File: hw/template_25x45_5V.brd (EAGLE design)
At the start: 25 x 45 mm, 25 parts, among them J1 GROVE-4P-2.0-3470130P1, J2 GROVE-4P-2.0-3470130P1, U5 LD3985XX

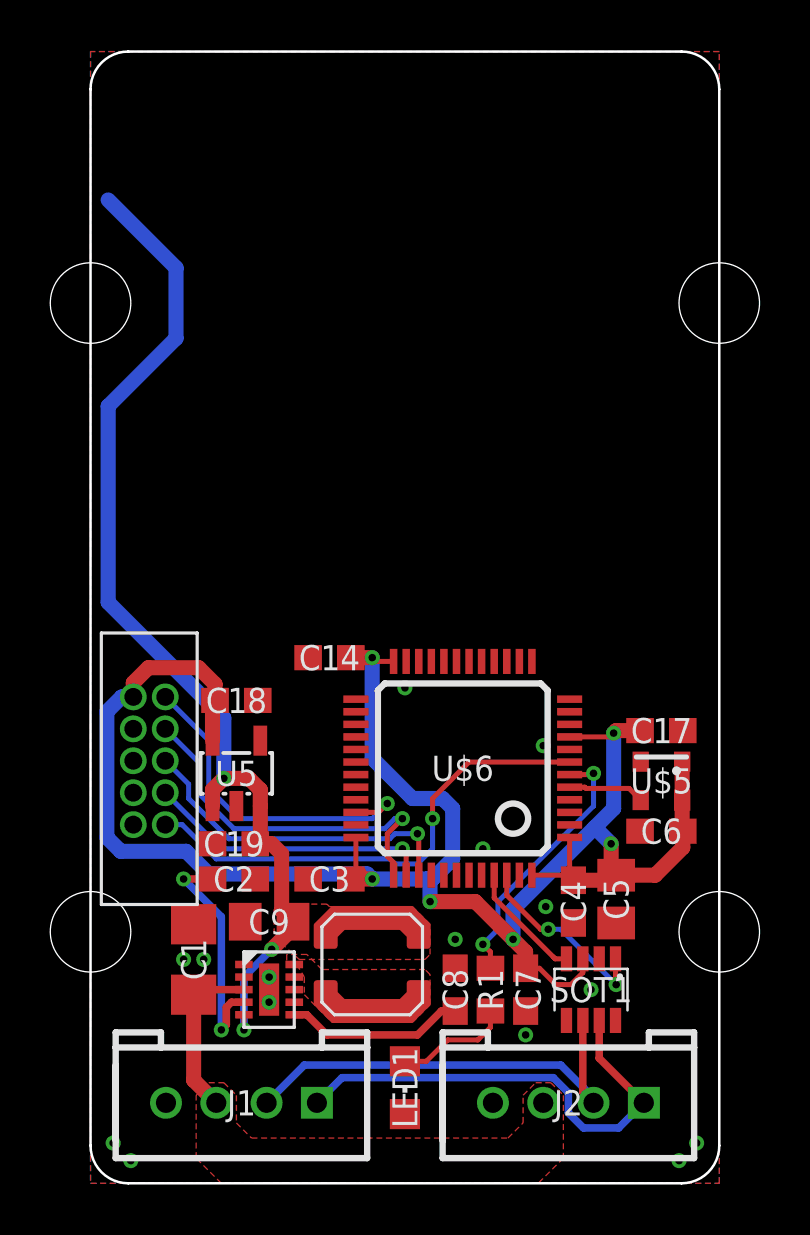
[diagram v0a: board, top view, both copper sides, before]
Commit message: Updated to R2P Eagle libraries
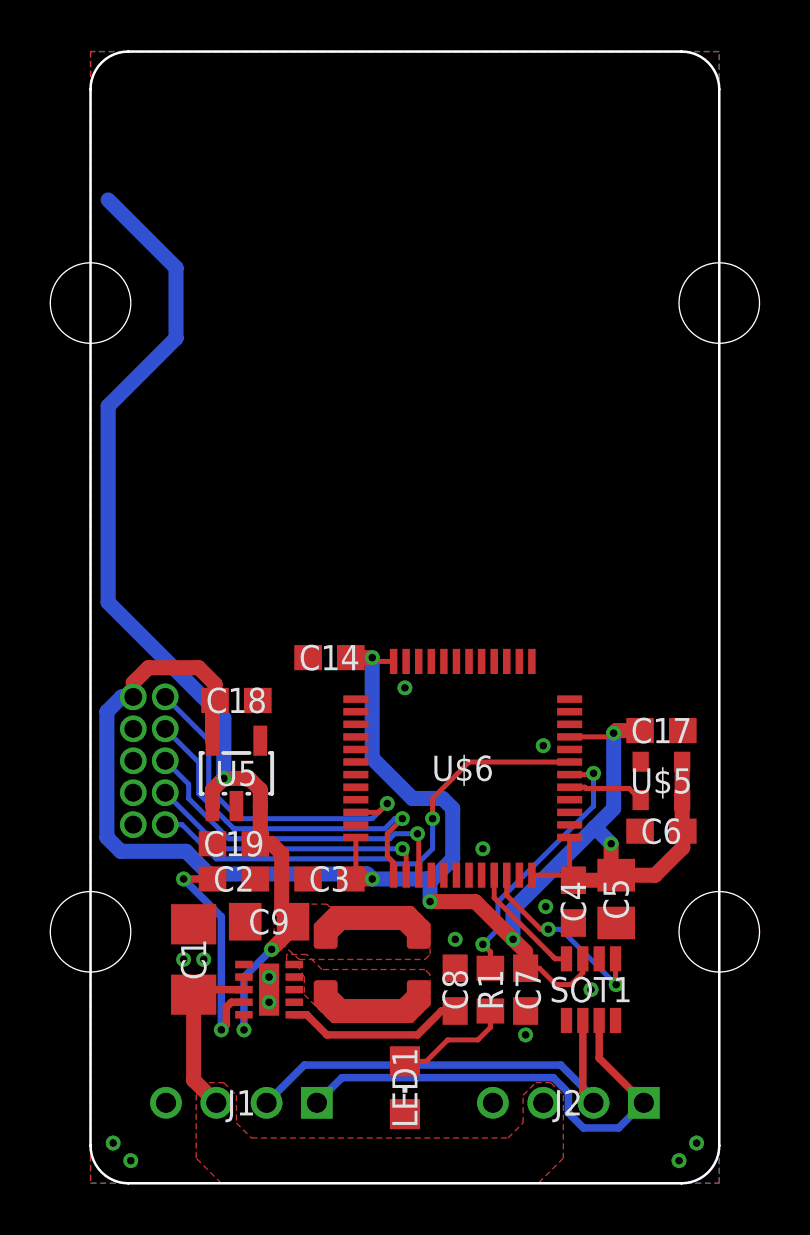
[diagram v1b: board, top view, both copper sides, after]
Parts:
- C1: value (none) -> 1u; device rcl:C1206 -> r2p_rcl:C1206
- C14, C17, C18, C19, C2, C3, C4, C6, C7, C8: device rcl:C0603 -> r2p_rcl:C0603
- C5: device rcl:C0805 -> r2p_rcl:C0805
- C9: value (none) -> 10u; device rcl:C0805 -> r2p_rcl:C0805
- J1, J2: value GROVE-4P-2.0-3470130P1 -> R2P_BUS-VERTICAL; device OPL Eagle Library:4P-2.0 -> r2p_connector:OPL-EAGLE-LIBRARY_4P-2.0
- LED1: device led:CHIPLED_0805 -> r2p_led:CHIPLED_0805
- R1: device rcl:R0603 -> r2p_rcl:R0603
- SOT1: device maxim:SOT23-8L -> r2p_ic:SOT23-8L
- U$2: device coilcraft:LPS4018 -> r2p_rcl:COILCRAFT_LPS4018
- U$3: device maxim:TDFN-10 -> r2p_ic:TDFN-10
- U$4: value FTSH-105TH -> JTAG-TH; device samtec:FTSH-105-TH -> r2p_connector:SAMTEC_FTSH-105-TH
- U$5: value ASD -> ABRACON_ASD; device abracon:2.5X2 -> r2p_ic:ABRACON_2.5X2
- U$6: value STM32F103CXTX -> STM32F303CTX; device st:LQFP48 -> r2p_ic:LQFP48
- U5: value LD3985XX -> TLV700XXDDC; device st:SOT23-5L -> r2p_ic:SOT23-5L
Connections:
- net VIN renamed +VBUS

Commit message: Updated keepout
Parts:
- U$2: value LPS4018 -> (none)
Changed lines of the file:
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@@
 <attribute name="VALUE" x="20.905" y="3.2" size="0.635" layer="27" font="vector" ratio="10" rot="R180"/>
 </element>
-<element name="U$2" library="r2p_rcl" package="COILCRAFT_LPS4018" value="LPS4018" x="11.2" y="8.7" smashed="yes" rot="R90"/>
+<element name="U$2" library="r2p_rcl" package="COILCRAFT_LPS4018" value="" x="11.2" y="8.7" smashed="yes" rot="R90"/>
 <element name="C1" library="r2p_rcl" package="C1206" value="1u" x="4.1" y="8.9" smashed="yes" rot="R90">
 <attribute name="NAME" x="4.1" y="8.9" size="1" layer="25" font="vector" rot="R90" align="center"/>
